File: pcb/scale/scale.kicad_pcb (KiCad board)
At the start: 2 copper layers, 103.8 x 47.9 mm, 89 parts, among them J1 USB_C_Receptacle_USB2.0, J2 Conn_01x07, J3 Conn_01x04, SW1 SW_Push, SW10 SW_Push, SW11 SW_Push, SW12 SW_Push, SW13 SW_Push, SW14 SW_Push, SW15 SW_Push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

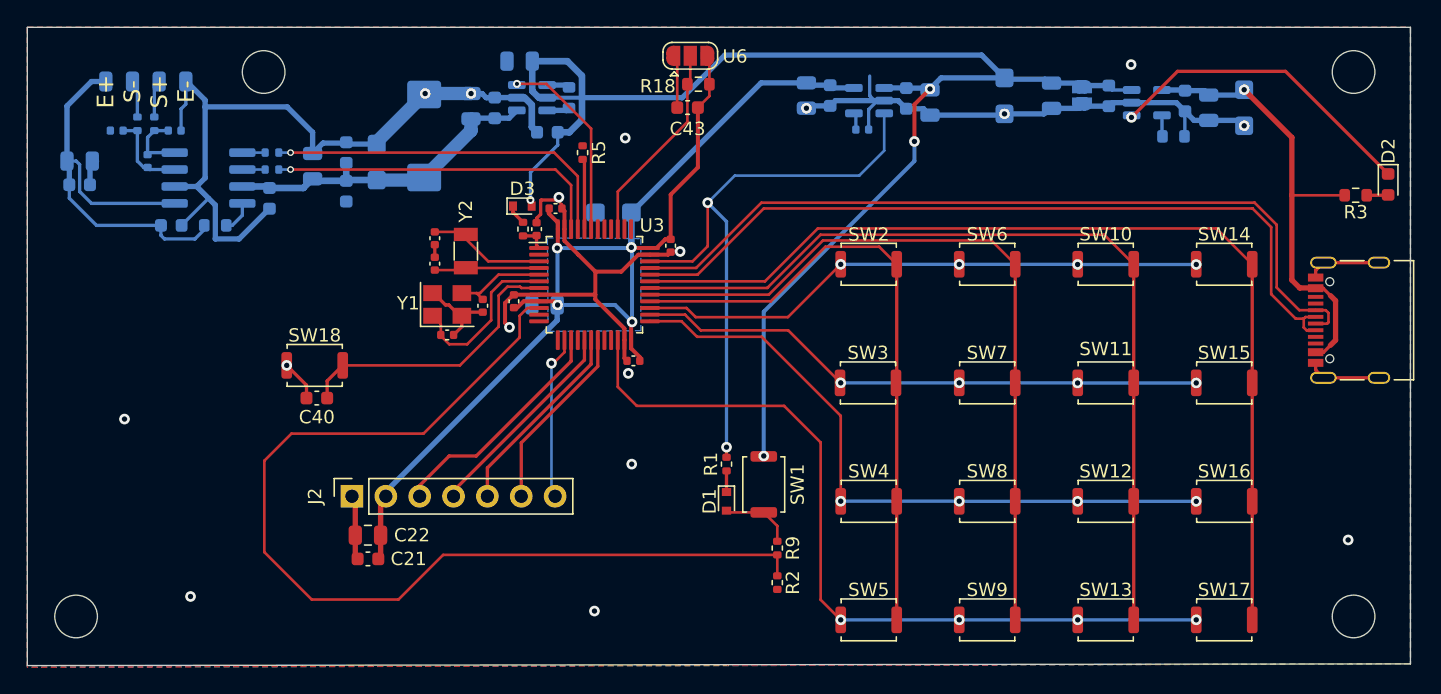
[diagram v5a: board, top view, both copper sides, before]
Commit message: 所有电源线增加到0.5mm
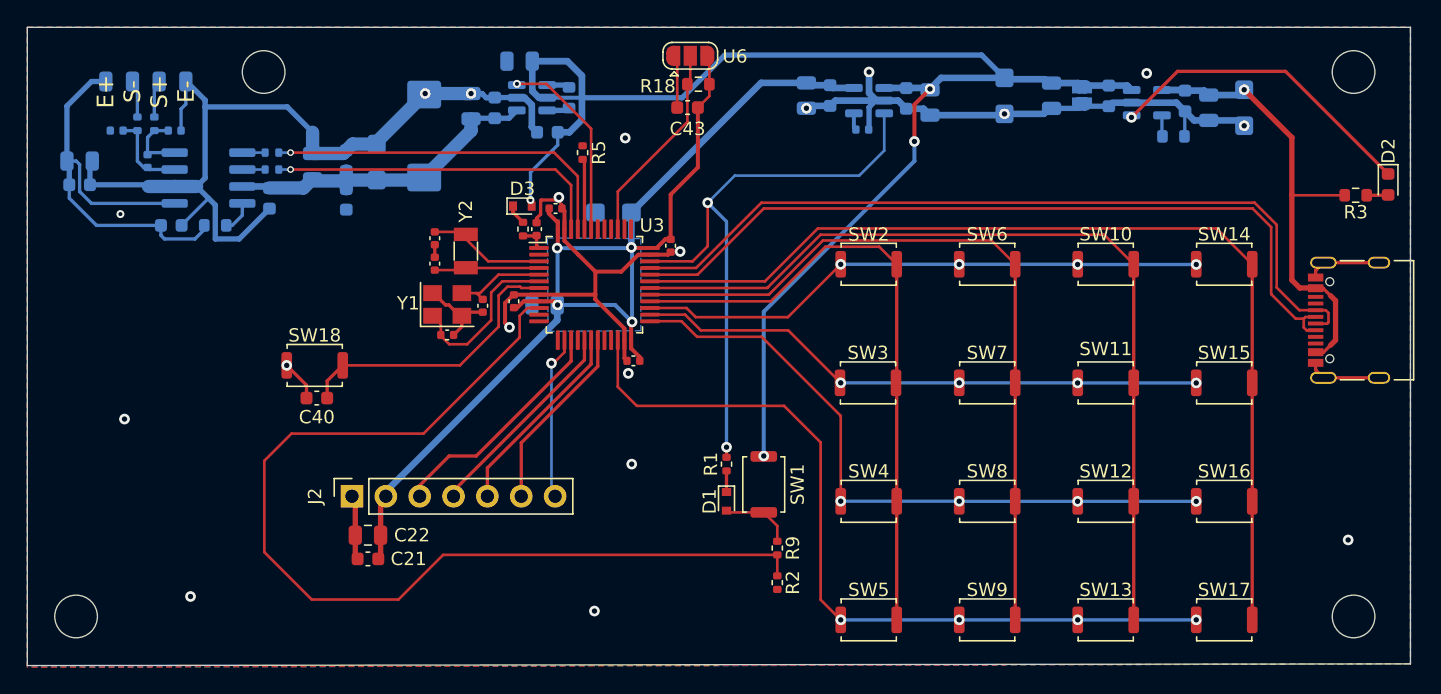
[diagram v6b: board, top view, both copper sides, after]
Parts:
- moved C41 0.61 mm to (93.0, 60.8)
- moved C42 0.61 mm to (93.0, 63.7)
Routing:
- net GND: track 165.9 -> 171.5 mm, vias 17 -> 19

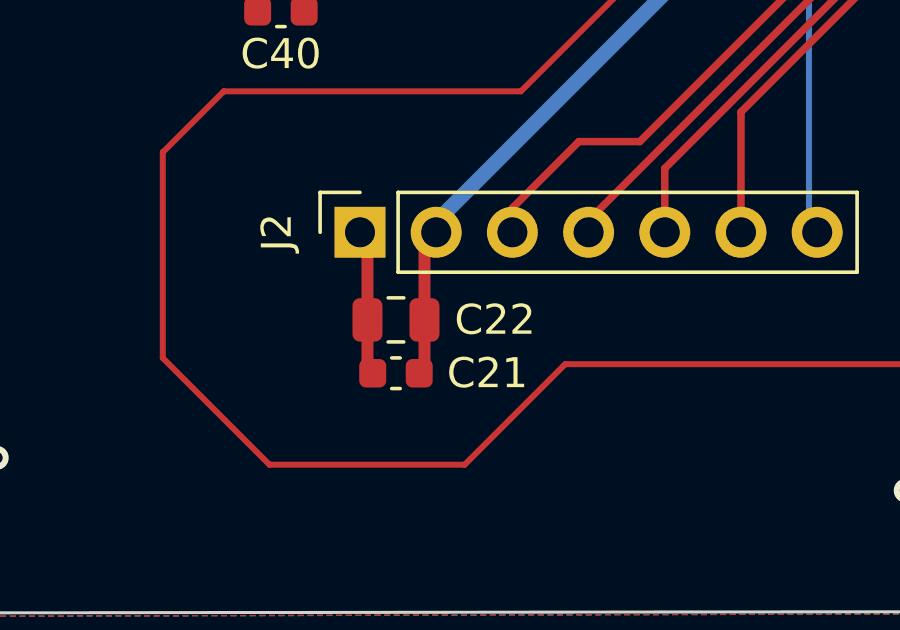
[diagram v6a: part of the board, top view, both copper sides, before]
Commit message: C22移动到背面
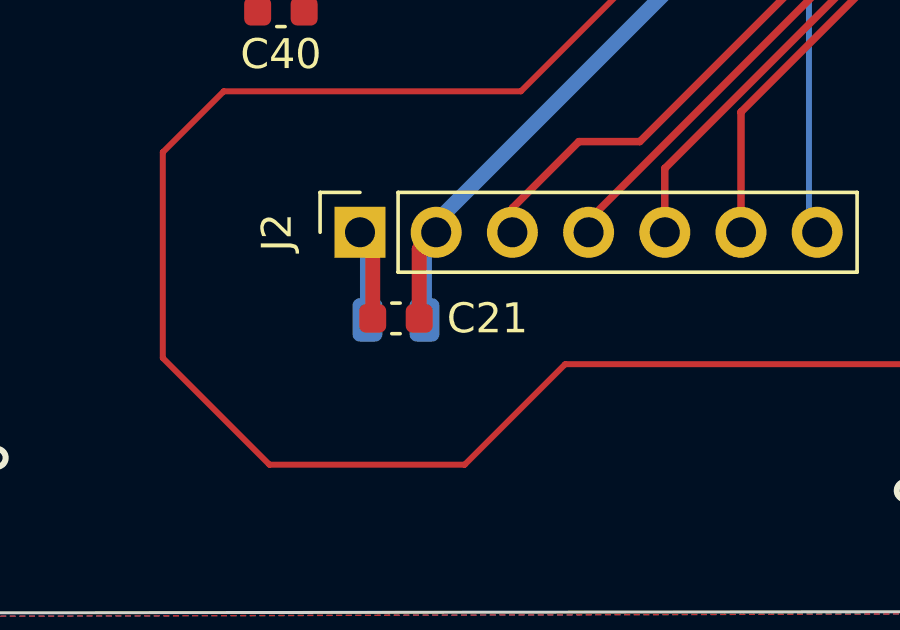
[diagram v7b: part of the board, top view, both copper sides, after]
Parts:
- C22: moved to B.Cu
- moved C21 1.83 mm to (94.6, 88.8)
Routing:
- net +3V3: track 98.1 -> 99.9 mm
- net GND: track 171.5 -> 173.0 mm
